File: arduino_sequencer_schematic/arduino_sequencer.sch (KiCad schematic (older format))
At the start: 160 parts, among them J1 AudioJack, J10 AudioJack, J11 AudioJack, J12 AudioJack, J13 AudioJack, J14 AudioJack, J15 AudioJack, J16 Conn_02x05, J2 AudioJack, J3 AudioJack, J4 AudioJack, J5 AudioJack, J6 AudioJack, J7 AudioJack, J8 AudioJack, J9 AudioJack, Q1 2N3904, Q10 2N3904, Q11 2N3904, Q2 2N3904, Q3 2N3904, Q4 2N3904, Q5 2N3904, Q6 2N3904, Q7 2N3904, Q8 2N3904, Q9 2N3904, SW1 SW_Push, SW2 SW_SPST, SW3 SW_Push, SW4 SW_Push, SW5 SW_SPST, SW6 SW_SPST, U1 74HC595, U2 TL084, U3 TL084, U4 L7805

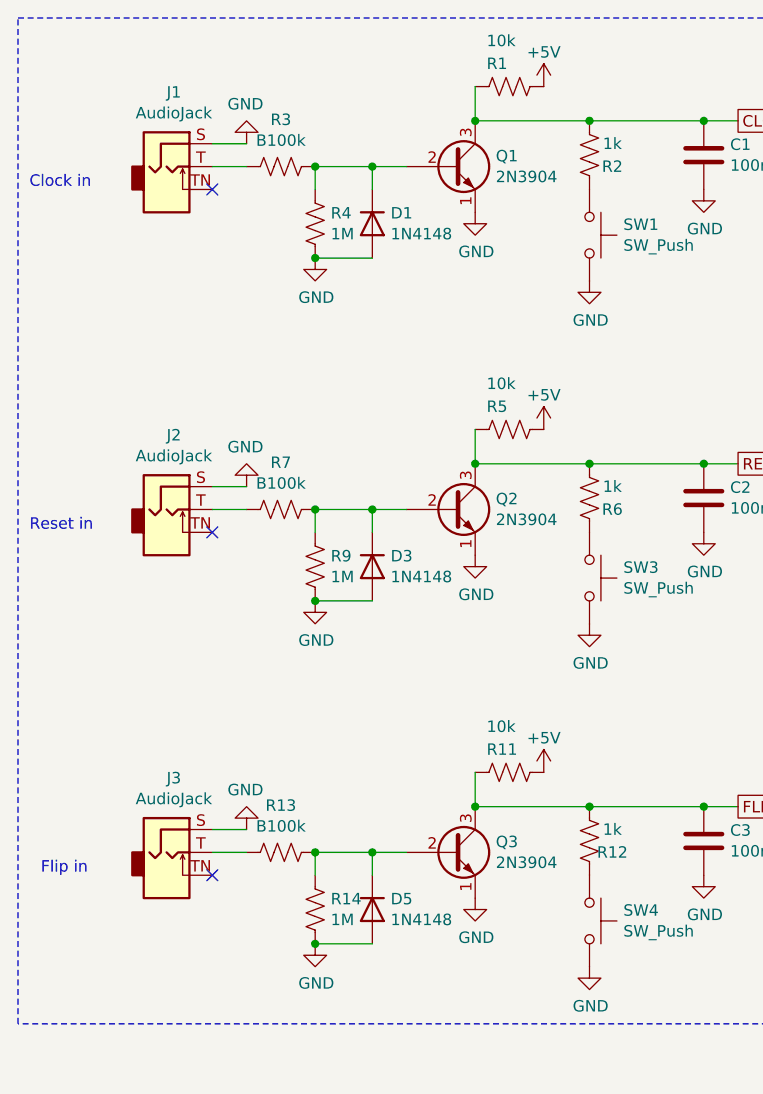
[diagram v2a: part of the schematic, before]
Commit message: Changed negative input protection diodes to Schottky diodes
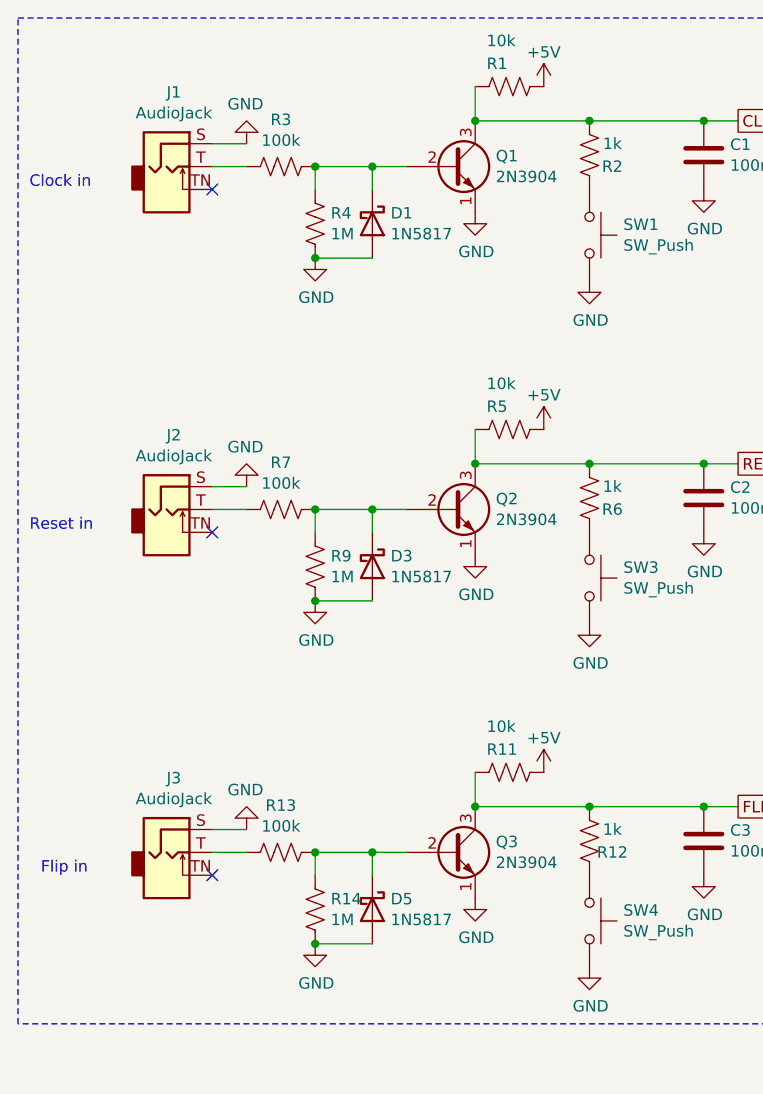
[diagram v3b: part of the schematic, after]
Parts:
- removed D1, D3, D5: 1N4148, Diode_THT:D_DO-35_SOD27_P7.62mm_Horizontal, symbol Diode:1N4148
- added D1, D3, D5: 1N5817, Diode_THT:D_DO-41_SOD81_P10.16mm_Horizontal, symbol Diode:1N5817
- R13, R3, R7: value B100k -> 100k
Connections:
- net GND: now also D1.2 (A), D3.2 (A), D5.2 (A)
- net at Q1.2 (B), R3.1, R4.1: now also D1.1 (K)
- net at Q2.2 (B), R7.1, R9.1: now also D3.1 (K)
- net at Q3.2 (B), R13.1, R14.1: now also D5.1 (K)
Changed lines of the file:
@@
 P 1800 2900
 F 0 "R7" V 1595 2900 50  0000 C CNN
-F 1 "B100k" V 1686 2900 50  0000 C CNN
+F 1 "100k" V 1686 2900 50  0000 C CNN
 F 2 "" V 1840 2890 50  0001 C CNN
 F 3 "~" H 1800 2900 50  0001 C CNN
@@
 P 1800 4400
 F 0 "R13" V 1595 4400 50  0000 C CNN
-F 1 "B100k" V 1686 4400 50  0000 C CNN
+F 1 "100k" V 1686 4400 50  0000 C CNN
 F 2 "" V 1840 4390 50  0001 C CNN
 F 3 "~" H 1800 4400 50  0001 C CNN
@@
 P 1800 1400
 F 0 "R3" V 1595 1400 50  0000 C CNN
-F 1 "B100k" V 1686 1400 50  0000 C CNN
+F 1 "100k" V 1686 1400 50  0000 C CNN
 F 2 "" V 1840 1390 50  0001 C CNN
 F 3 "~" H 1800 1400 50  0001 C CNN
@@
 	0    1    1    0
 $EndComp
-$Comp
-L Diode:1N4148 D5
-U 1 1 5FD05317
-P 2200 4650
-F 0 "D5" V 2154 4730 50  0000 L CNN
-F 1 "1N4148" V 2245 4730 50  0000 L CNN
-F 2 "Diode_THT:D_DO-35_SOD27_P7.62mm_Horizontal" H 2200 4475 50  0001 C CNN
-F 3 "https://assets.nexperia.com/documents/data-sheet/1N4148_1N4448.pdf" H 2200 4650 50  0001 C CNN
-	1    2200 4650
-	0    1    1    0
-$EndComp
-$Comp
-L Diode:1N4148 D3
-U 1 1 5FD07A77
-P 2200 3150
-F 0 "D3" V 2154 3230 50  0000 L CNN
-F 1 "1N4148" V 2245 3230 50  0000 L CNN
-F 2 "Diode_THT:D_DO-35_SOD27_P7.62mm_Horizontal" H 2200 2975 50  0001 C CNN
-F 3 "https://assets.nexperia.com/documents/data-sheet/1N4148_1N4448.pdf" H 2200 3150 50  0001 C CNN
-	1    2200 3150
-	0    1    1    0
-$EndComp
-$Comp
-L Diode:1N4148 D1
-U 1 1 5FD0988E
-P 2200 1650
-F 0 "D1" V 2154 1730 50  0000 L CNN
-F 1 "1N4148" V 2245 1730 50  0000 L CNN
-F 2 "Diode_THT:D_DO-35_SOD27_P7.62mm_Horizontal" H 2200 1475 50  0001 C CNN
-F 3 "https://assets.nexperia.com/documents/data-sheet/1N4148_1N4448.pdf" H 2200 1650 50  0001 C CNN
-	1    2200 1650
-	0    1    1    0
-$EndComp
 Wire Wire Line
 	2200 1500 2200 1400
@@
 Wire Wire Line
 	2050 6200 2050 6550
+$Comp
+L Diode:1N5817 D1
+U 1 1 5FD809C8
+P 2200 1650
+F 0 "D1" V 2154 1730 50  0000 L CNN
+F 1 "1N5817" V 2245 1730 50  0000 L CNN
+F 2 "Diode_THT:D_DO-41_SOD81_P10.16mm_Horizontal" H 2200 1475 50  0001 C CNN
+F 3 "http://www.vishay.com/docs/88525/1n5817.pdf" H 2200 1650 50  0001 C CNN
+	1    2200 1650
+	0    1    1    0
+$EndComp
+$Comp
+L Diode:1N5817 D3
+U 1 1 5FD81667
+P 2200 3150
+F 0 "D3" V 2154 3230 50  0000 L CNN
+F 1 "1N5817" V 2245 3230 50  0000 L CNN
+F 2 "Diode_THT:D_DO-41_SOD81_P10.16mm_Horizontal" H 2200 2975 50  0001 C CNN
+F 3 "http://www.vishay.com/docs/88525/1n5817.pdf" H 2200 3150 50  0001 C CNN
+	1    2200 3150
+	0    1    1    0
+$EndComp
+$Comp
+L Diode:1N5817 D5
+U 1 1 5FD821C4
+P 2200 4650
+F 0 "D5" V 2154 4730 50  0000 L CNN
+F 1 "1N5817" V 2245 4730 50  0000 L CNN
+F 2 "Diode_THT:D_DO-41_SOD81_P10.16mm_Horizontal" H 2200 4475 50  0001 C CNN
+F 3 "http://www.vishay.com/docs/88525/1n5817.pdf" H 2200 4650 50  0001 C CNN
+	1    2200 4650
+	0    1    1    0
+$EndComp
 $EndSCHEMATC

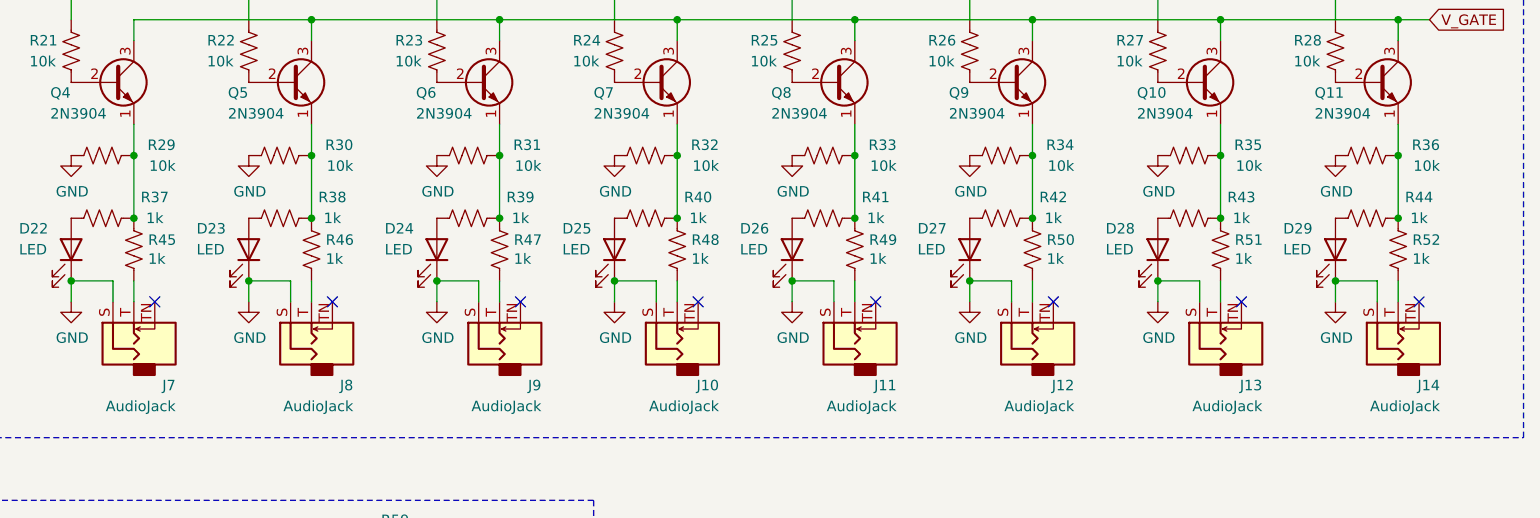
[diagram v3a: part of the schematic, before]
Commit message: Fixed gate output resistors
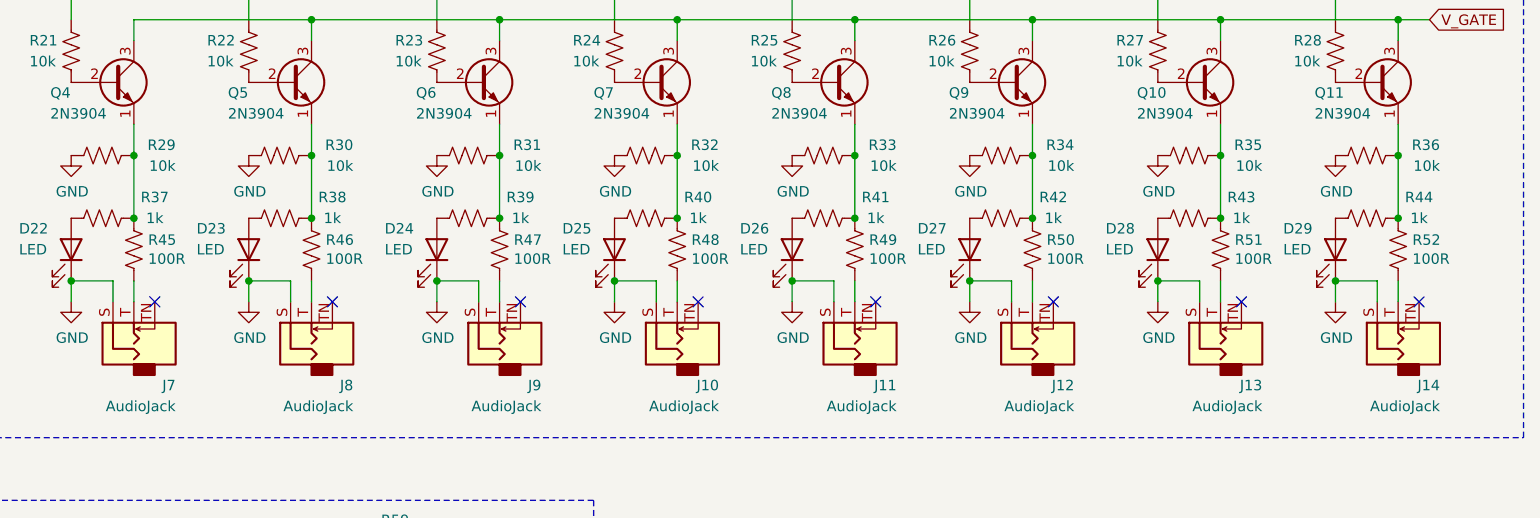
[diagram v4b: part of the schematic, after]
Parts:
- R45, R46, R47, R48, R49, R50, R51, R52: value 1k -> 100R
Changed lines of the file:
@@
 P 8450 8250
 F 0 "R45" H 8518 8296 50  0000 L CNN
-F 1 "1k" H 8518 8205 50  0000 L CNN
+F 1 "100R" H 8518 8205 50  0000 L CNN
 F 2 "" V 8490 8240 50  0001 C CNN
 F 3 "~" H 8450 8250 50  0001 C CNN
@@
 P 9300 8250
 F 0 "R46" H 9368 8296 50  0000 L CNN
-F 1 "1k" H 9368 8205 50  0000 L CNN
+F 1 "100R" H 9368 8205 50  0000 L CNN
 F 2 "" V 9340 8240 50  0001 C CNN
 F 3 "~" H 9300 8250 50  0001 C CNN
@@
 P 10200 8250
 F 0 "R47" H 10268 8296 50  0000 L CNN
-F 1 "1k" H 10268 8205 50  0000 L CNN
+F 1 "100R" H 10268 8205 50  0000 L CNN
 F 2 "" V 10240 8240 50  0001 C CNN
 F 3 "~" H 10200 8250 50  0001 C CNN
@@
 P 11050 8250
 F 0 "R48" H 11118 8296 50  0000 L CNN
-F 1 "1k" H 11118 8205 50  0000 L CNN
+F 1 "100R" H 11118 8205 50  0000 L CNN
 F 2 "" V 11090 8240 50  0001 C CNN
 F 3 "~" H 11050 8250 50  0001 C CNN
@@
 P 11900 8250
 F 0 "R49" H 11968 8296 50  0000 L CNN
-F 1 "1k" H 11968 8205 50  0000 L CNN
+F 1 "100R" H 11968 8205 50  0000 L CNN
 F 2 "" V 11940 8240 50  0001 C CNN
 F 3 "~" H 11900 8250 50  0001 C CNN
@@
 P 12750 8250
 F 0 "R50" H 12818 8296 50  0000 L CNN
-F 1 "1k" H 12818 8205 50  0000 L CNN
+F 1 "100R" H 12818 8205 50  0000 L CNN
 F 2 "" V 12790 8240 50  0001 C CNN
 F 3 "~" H 12750 8250 50  0001 C CNN
@@
 P 13650 8250
 F 0 "R51" H 13718 8296 50  0000 L CNN
-F 1 "1k" H 13718 8205 50  0000 L CNN
+F 1 "100R" H 13718 8205 50  0000 L CNN
 F 2 "" V 13690 8240 50  0001 C CNN
 F 3 "~" H 13650 8250 50  0001 C CNN
@@
 P 14500 8250
 F 0 "R52" H 14568 8296 50  0000 L CNN
-F 1 "1k" H 14568 8205 50  0000 L CNN
+F 1 "100R" H 14568 8205 50  0000 L CNN
 F 2 "" V 14540 8240 50  0001 C CNN
 F 3 "~" H 14500 8250 50  0001 C CNN

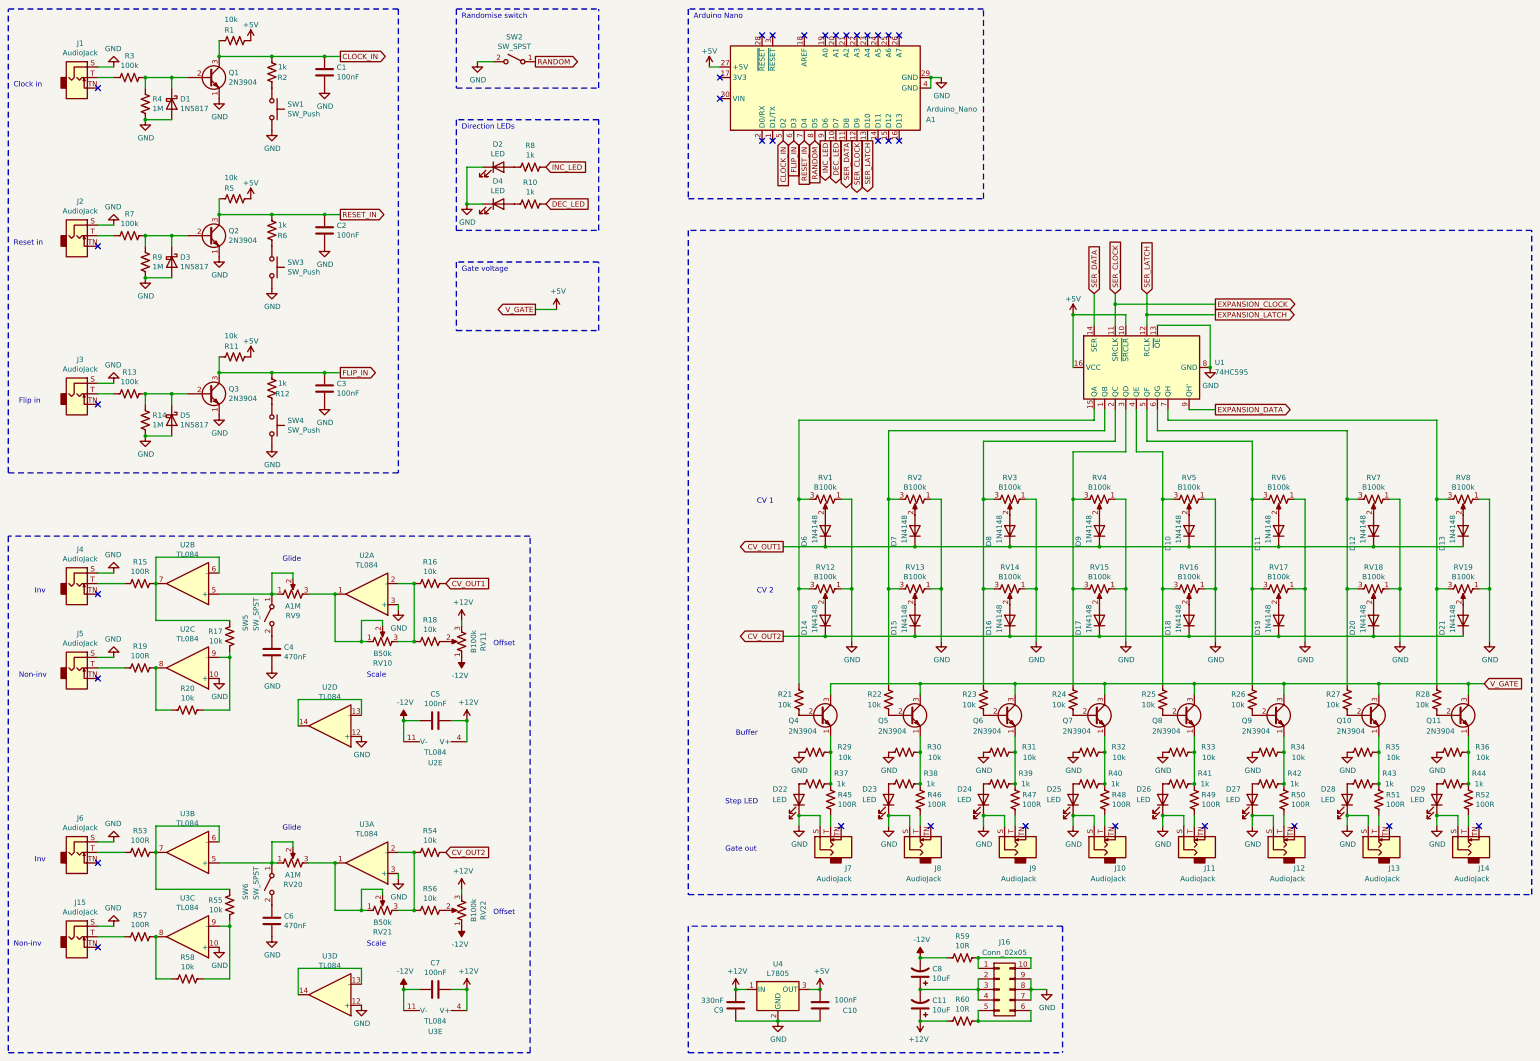
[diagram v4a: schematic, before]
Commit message: Added additional LEDs
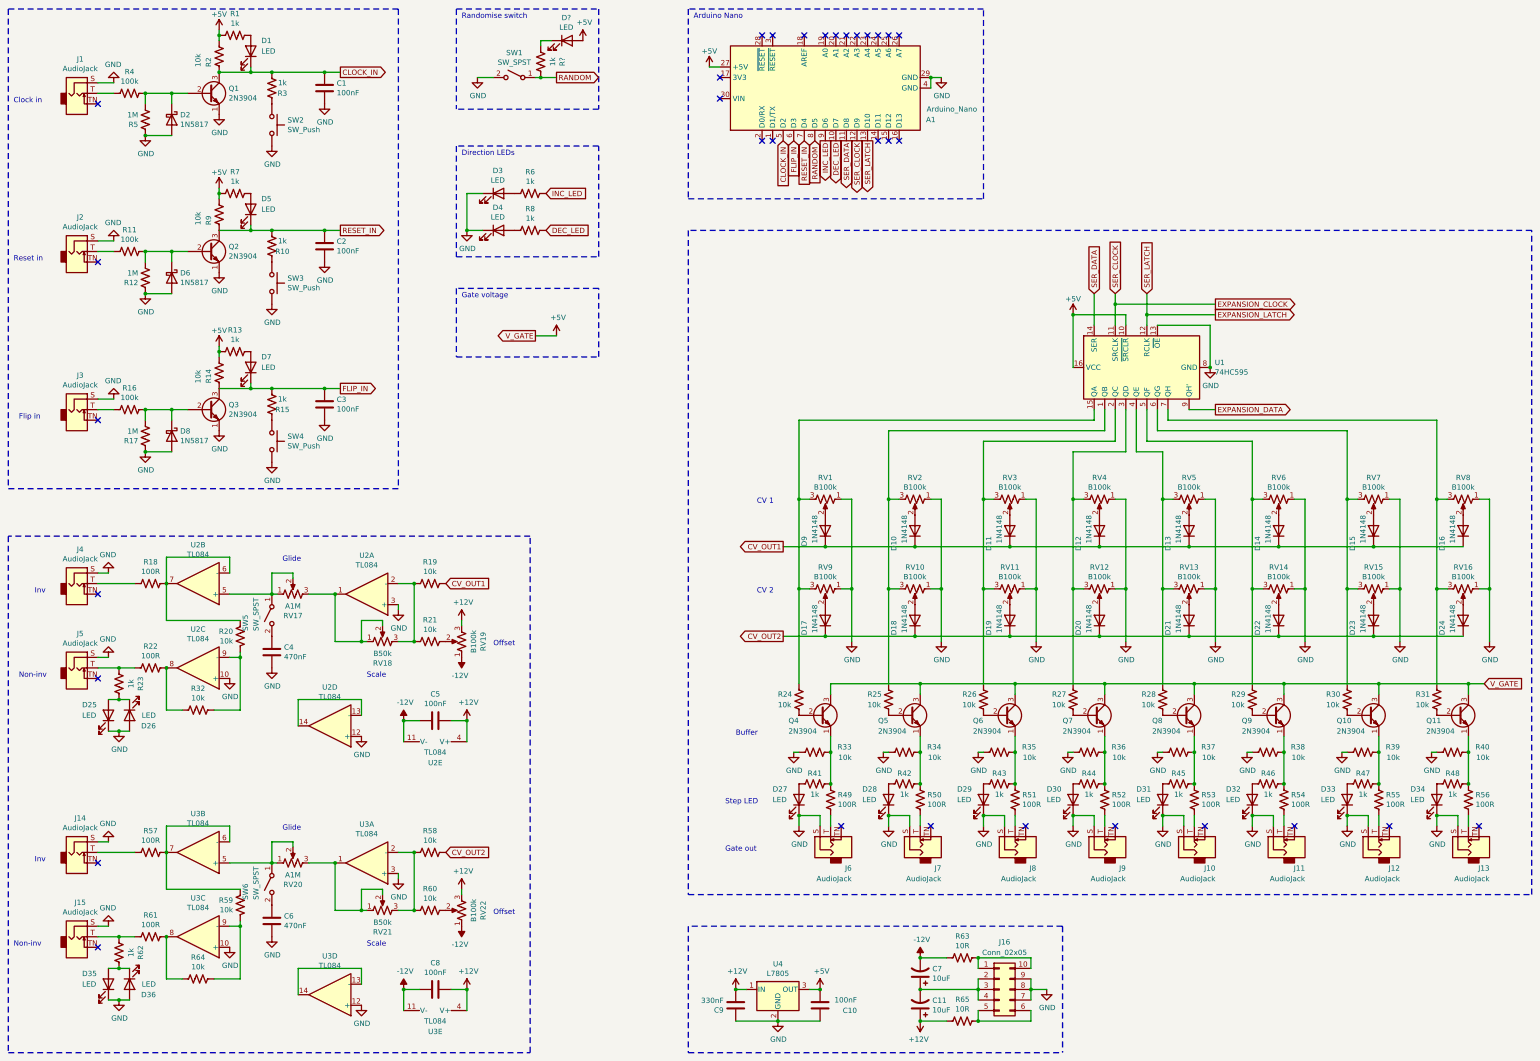
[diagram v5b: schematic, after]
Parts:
- removed R11, R5: 10k, symbol Device:R_US
- added D1, D25, D26, D35, D36, D5, D7, D?: LED, symbol Device:LED
- added R1, R13, R23, R62, R7, R?: 1k, symbol Device:R_US
- added R14, R9: 10k, symbol Device:R_US
- renumbered C8 to C7, C7 to C8, D7 to D10, D8 to D11, D9 to D12, D10 to D13, D11 to D14, D12 to D15, D13 to D16, D14 to D17, D15 to D18, D16 to D19, D1 to D2, D17 to D20, D18 to D21, D19 to D22, D20 to D23, D21 to D24, D22 to D27, D23 to D28, D24 to D29, D2 to D3, D25 to D30, D26 to D31, D27 to D32, D28 to D33, D29 to D34, D3 to D6, D5 to D8, D6 to D9, J11 to J10, J12 to J11, J13 to J12, J14 to J13, J6 to J14, J7 to J6, J8 to J7, J9 to J8, J10 to J9, R6 to R10, R7 to R11, R9 to R12, R12 to R15, R13 to R16, R14 to R17, R15 to R18, R16 to R19, R1 to R2, R17 to R20, R18 to R21, R19 to R22, R21 to R24, R22 to R25, R23 to R26, R24 to R27, R25 to R28, R26 to R29, R2 to R3, R27 to R30, R28 to R31, R20 to R32, R29 to R33, R30 to R34, R31 to R35, R32 to R36, R33 to R37, R34 to R38, R35 to R39, R3 to R4, R36 to R40, R37 to R41, R38 to R42, R39 to R43, R40 to R44, R41 to R45, R42 to R46, R43 to R47, R44 to R48, R45 to R49, R4 to R5, R46 to R50, R47 to R51, R48 to R52, R49 to R53, R50 to R54, R51 to R55, R52 to R56, R53 to R57, R54 to R58, R55 to R59, R8 to R6, R56 to R60, R57 to R61, R59 to R63, R58 to R64, R60 to R65, R10 to R8, RV13 to RV10, RV14 to RV11, RV15 to RV12, RV16 to RV13, RV17 to RV14, RV18 to RV15, RV19 to RV16, RV9 to RV17, RV10 to RV18, RV11 to RV19, RV12 to RV9, SW2 to SW1, SW1 to SW2
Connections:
- net +5V: now also D?.2 (A), R1.2, R13.2, R14.1, R7.2, R9.1
- net CLOCK_IN: now also D1.1 (K)
- net FLIP_IN: now also D7.1 (K), R14.2
- net GND: now also R12.1, R17.1, R5.1, D25.1 (K), D26.2 (A), D35.1 (K), D36.2 (A); no longer R12.2, R17.2, R5.2
- net RANDOM: now also R?.1
- net RESET_IN: now also D5.1 (K), R9.2
- net at D2.1 (K), Q1.2 (B), R4.1: now also R5.2; no longer R5.1
- net at D6.1 (K), Q2.2 (B), R11.1: now also R12.2; no longer R12.1
- net at D8.1 (K), Q3.2 (B), R16.1: now also R17.2; no longer R17.1
- net at J15.T, R61.2: now also R62.2
- net at J5.T, R22.2: now also R23.2
- new net: D25.2 (A), D26.1 (K), R23.1
- new net: D35.2 (A), D36.1 (K), R62.1
- new net: D1.2 (A), R1.1
- new net: D5.2 (A), R7.1
- new net: D7.2 (A), R13.1
- new net: D?.1 (K), R?.2
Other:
- moved on the sheet: C1, C2, C3, D2, D3, D4, D6, D8, J1, J2, J3, Q1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
